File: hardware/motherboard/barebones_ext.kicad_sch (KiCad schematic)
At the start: 30 parts, among them J24 FH12-30S-0.5SH_55_, SW1 EC05E1220401, SW2 EC05E1220401, SW3 EC05E1220401, U36 STM32F411CEU6

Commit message: arranged the schematics in every sheet
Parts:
- removed R203: 100k, Resistor_SMD:R_0603_1608Metric, symbol Device:R
- removed R225: 1k, Resistor_SMD:R_0603_1608Metric, symbol Device:R
- removed R236: 10k, Resistor_SMD:R_0603_1608Metric, symbol Device:R
- removed S5: TL3342F160QG, barebones:SW_TL3342F160QG, symbol TL3342F160QG:TL3342F160QG
- added C419: 4.7uF, Capacitor_SMD:C_0603_1608Metric, symbol Device:C
- added C422, C424, C430, C434, C465, C467: 0.1uF, Capacitor_SMD:C_0603_1608Metric, symbol Device:C
- added C435, C466: 10uF, Capacitor_SMD:C_0603_1608Metric, symbol Device:C
- added C601, C602: 12pF, Capacitor_SMD:C_0201_0603Metric, symbol Device:C
- added R249, R250: 10k, Resistor_SMD:R_0603_1608Metric, symbol Device:R
- added SW4, SW6: SW_Push, symbol Switch:SW_Push
- added TP2: 3V3, TestPoint:TestPoint_Pad_D1.0mm, symbol Connector:TestPoint
- added TP3: BOOT0, TestPoint:TestPoint_Pad_D1.0mm, symbol Connector:TestPoint
- added TP4: NRST, TestPoint:TestPoint_Pad_D1.0mm, symbol Connector:TestPoint
- added TP7: SWDIO, TestPoint:TestPoint_Pad_D1.0mm, symbol Connector:TestPoint
- added TP8: SWCLK, TestPoint:TestPoint_Pad_D1.0mm, symbol Connector:TestPoint
- added Y8: C2E-25.000-10-1530-X-R, barebones:XTAL_C2E-25.000-10-1530-X-R, symbol C2E-25.000-10-1530-X-R:C2E-25.000-10-1530-X-R
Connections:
- net DC/SCL is gone; now on net SPI_SCK: U36.15 (PA5)
- net SDA is gone; now on net SPI_MOSI: U36.17 (PA7)
- net VDD is gone; now on net VCC_3V3_SYS: U36.24 (VDD), U36.36 (VDD), U36.48 (VDD)
- net BOOT0: now also R249.2, SW4.1, TP3.1
- net EN_BTN_0: now also U36.39 (PB3); no longer R233.1, R238.1, SW2.5, SW3.5
- net EN_CHAN_A_0: now also U36.19 (PB1)
- net EN_CHAN_A_1: now also U36.41 (PB5)
- net EN_CHAN_A_2: now also U36.45 (PB8)
- net EN_CHAN_B_0: now also U36.18 (PB0)
- net EN_CHAN_B_1: now also U36.40 (PB4)
- net EN_CHAN_B_2: now also U36.43 (PB7)
- net GND: now also C419.2, C422.2, C424.2, C430.2, C434.2, C435.2, C465.2, C466.2, C467.2, C601.1, C602.1, R249.1, R250.1, SW6.2, Y8.2 (GND), Y8.4 (GND)
- net LED_CS: now also U36.14 (PA4)
- net LED_DC: now also U36.13 (PA3)
- net LED_RES: now also U36.12 (PA2)
- net PRG_BTN_0: now also U36.21 (PB10)
- net PRG_BTN_1: now also U36.25 (PB12)
- net PRG_BTN_2: now also U36.26 (PB13)
- net VCC_3V3_SYS: now also U36.1 (VBAT), U36.9 (VREF+), C424.1, C430.1, C434.1, C435.1, C465.1, C466.1, C467.1, SW4.2, TP2.1
- net at U36.10 (PA0-WKUP): now also R250.2
- net at U36.22 (VCAP_1): now also C419.1
- net USB_VBUS: now reaches U36.30 (PA9)
- net USB_MACRO_DN: now reaches U36.32 (PA11)
- net USB_MACRO_DP: now reaches U36.33 (PA12)
- net SWDIO: now reaches U36.34 (PA13)
- net SWDIO: now also TP7.1
- net SWCLK: now reaches U36.37 (PA14)
- net SWCLK: now also TP8.1
- net EN_BTN_1: now reaches U36.42 (PB6)
- net EN_BTN_1: now also R233.1, SW2.5
- net EN_BTN_2: now reaches U36.46 (PB9)
- net EN_BTN_2: now also R238.1, SW3.5
- net XTALI: now reaches U36.5 (PH0-OSC_IN)
- net XTALI: now also C601.2, Y8.3
- net XTALO: now reaches U36.6 (PH1-OSC_OUT)
- net XTALO: now also C602.2, Y8.1
- net NRST: now reaches U36.7 (NRST)
- net NRST: now also C422.1, SW6.1, TP4.1
- no-connect marks 10 -> 20
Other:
- note added: "1.9" DISPLAY CONNECTOR"
- note added: "STM32F411 MCU"
- note added: "VDD CAPS"
- note added: "VREF+ CAPS"
- note removed: "POWER BUTTON"
- moved on the sheet: C409, C410, C416, C417, C421, J24, R137, R139, R142, R228, R229, R230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

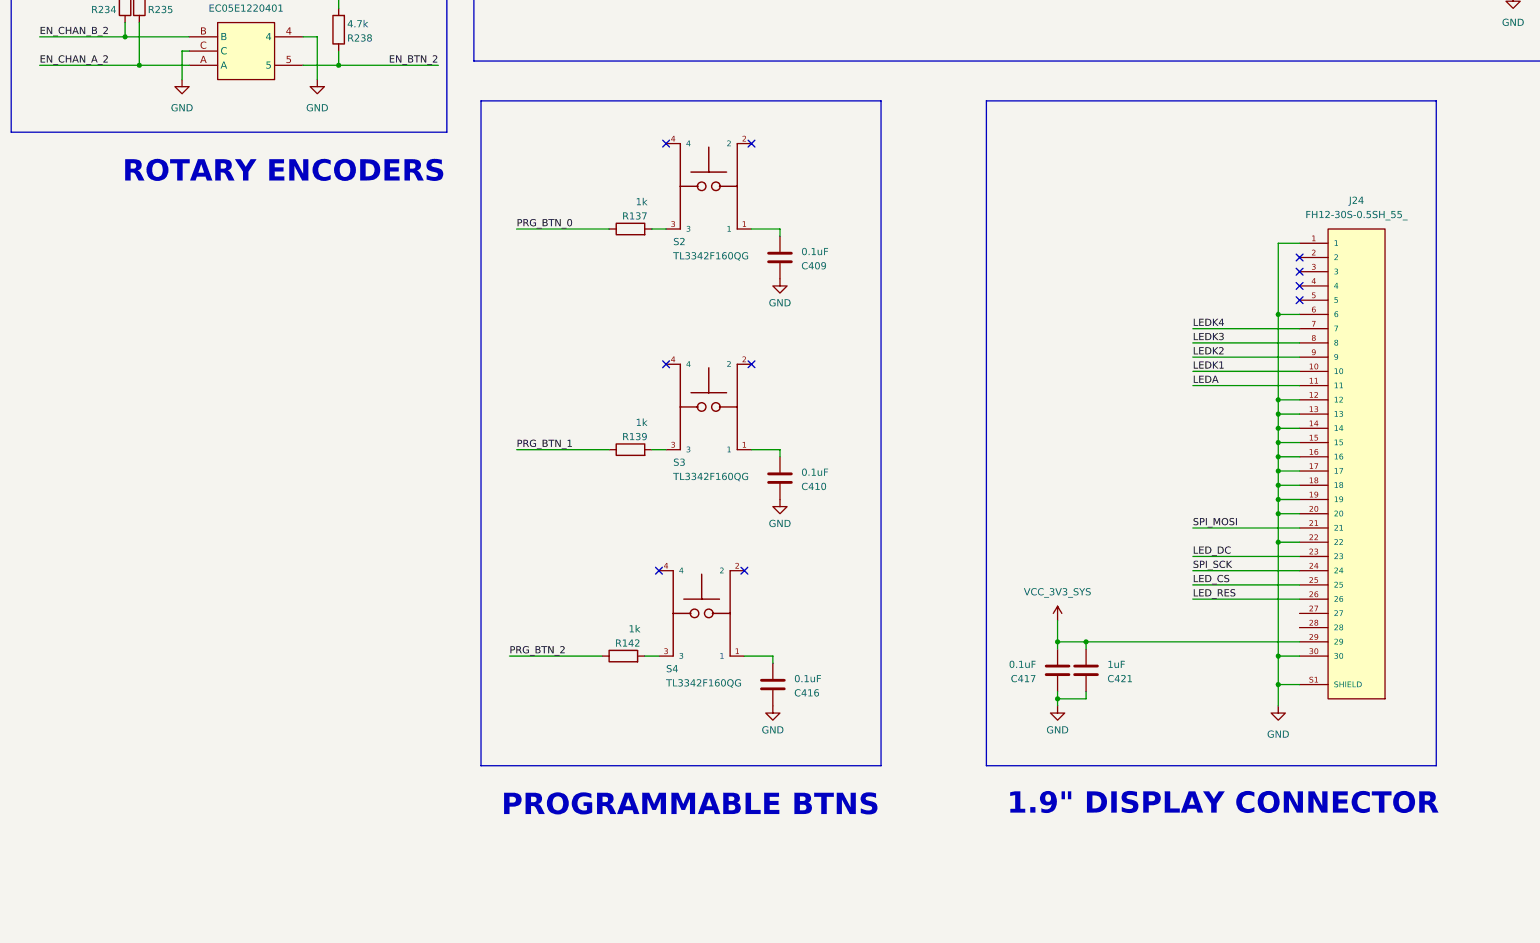
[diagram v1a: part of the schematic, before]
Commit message: removed unused components and connections
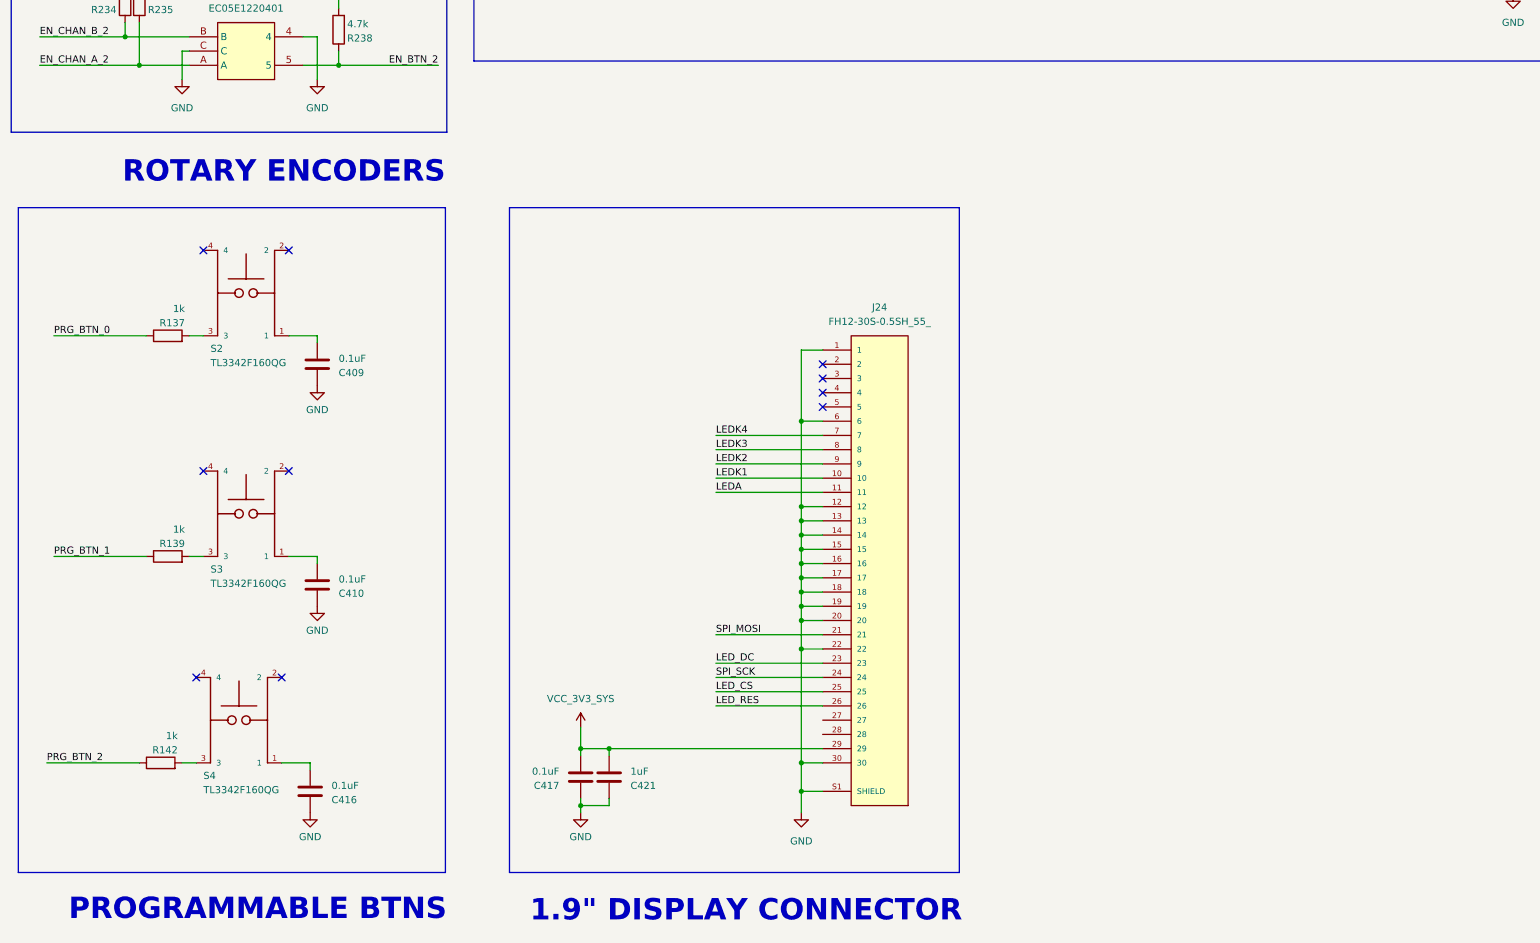
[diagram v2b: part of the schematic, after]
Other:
- moved on the sheet: C409, C410, C416, C417, C421, J24, R137, R139, R142, S2, S3, S4

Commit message: updated last changes
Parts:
- removed C417: 0.1uF, Capacitor_SMD:C_0603_1608Metric, symbol Device:C
- removed C421: 1uF, Capacitor_SMD:C_0603_1608Metric, symbol Device:C
- removed C601: 12pF, Capacitor_SMD:C_0201_0603Metric, symbol Device:C
- removed R228: 4.7k, Resistor_SMD:R_0402_1005Metric, symbol Device:R
- removed SW4, SW6: SW_Push, symbol Switch:SW_Push
- added C539: 0.1uF, Capacitor_SMD:C_0201_0603Metric, symbol Device:C
- added C546: 1uF, Capacitor_SMD:C_0201_0603Metric, symbol Device:C
- added C623: 12pF, Capacitor_SMD:C_0201_0603Metric, symbol Device:C
- added R236: 4.7k, Resistor_SMD:R_0201_0603Metric, symbol Device:R
- added S5, S6: TL3342F160QG, barebones:SW_TL3342F160QG, symbol TL3342F160QG:TL3342F160QG
- C409, C410, C416, C419, C422, C424, C430, C434, C465, C466, C467: footprint Capacitor_SMD:C_0603_1608Metric -> Capacitor_SMD:C_0201_0603Metric
- C435: value 10uF -> 0.1uF; footprint Capacitor_SMD:C_0603_1608Metric -> Capacitor_SMD:C_0201_0603Metric
- C602: KiLib_Generator (none) -> SMD_2terminal_chip_molded
- J24: footprint FH12-30S-0.5SH_55_:HIROSE_FH12-30S-0.5SH_55_ -> barebones:HIROSE_FH12-30S-0.5SH_55_
- R137, R139, R142, R237, R249, R250: footprint Resistor_SMD:R_0603_1608Metric -> Resistor_SMD:R_0201_0603Metric
- R229, R230, R231, R232, R233, R234, R235, R238: footprint Resistor_SMD:R_0402_1005Metric -> Resistor_SMD:R_0201_0603Metric
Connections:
- net LEDK2 is gone; now on net GND: J24.9
- net LEDK3 is gone; now on net SPI_DC: J24.8
- net USB_VBUS is gone; now on net EN_CHAN_A_0: U36.30 (PA9)
- net BOOT0: now also S6.3
- net EN_BTN_0: now also U36.31 (PA10); no longer U36.39 (PB3)
- net EN_BTN_1: now also U36.41 (PB5); no longer U36.42 (PB6)
- net EN_BTN_2: now also R234.1, U36.21 (PB10); no longer R238.1, U36.46 (PB9)
- net EN_CHAN_A_0: no longer U36.19 (PB1)
- net EN_CHAN_A_1: now also U36.40 (PB4); no longer U36.41 (PB5)
- net EN_CHAN_A_2: now also U36.46 (PB9); no longer U36.45 (PB8)
- net EN_CHAN_B_0: now also U36.29 (PA8), R236.1; no longer U36.18 (PB0)
- net EN_CHAN_B_1: now also U36.39 (PB3); no longer U36.40 (PB4)
- net EN_CHAN_B_2: now also R238.1, U36.45 (PB8); no longer R234.1, U36.43 (PB7)
- net GND: now also J24.11, J24.25, C539.2, C546.2, C623.1, S5.1; no longer J24.19, J24.20, J24.22, J24.6
- net LEDA: now also J24.20; no longer J24.11
- net NRST: now also S5.3
- net PRG_BTN_0: now also U36.25 (PB12); no longer U36.21 (PB10)
- net PRG_BTN_1: now also U36.26 (PB13); no longer U36.25 (PB12)
- net PRG_BTN_2: now also U36.27 (PB14); no longer U36.26 (PB13)
- net XTALI: now also C623.2
- net VCC_3V3_S3: now reaches J24.2
- net VCC_3V3_S3: now also C424.1, C430.1, C434.1, C435.1, C465.1, C466.1, C467.1, J24.3, J24.4, R229.2, R230.2, R231.2, R232.2, R233.2, R234.2, R235.2, R238.2, TP2.1, U36.1 (VBAT), U36.24 (VDD), U36.36 (VDD), U36.48 (VDD), U36.9 (VREF+), C539.1, C546.1, R236.2, S6.1
- net CTP_SCL: now reaches J24.27
- net CTP_SCL: now also U36.42 (PB6)
- net CTP_SDA: now reaches J24.28
- net CTP_SDA: now also U36.43 (PB7)
- net RESET: now reaches J24.5
- net RESET: now also U36.12 (PA2)
- net SPI_DC: now reaches U36.16 (PA6)
- net LEDK1 renamed MOSI
- net MOSI: now also U36.17 (PA7)
- net LEDK4 renamed SCLK
- net SCLK: now also U36.15 (PA5)
- net LED_CS renamed CS
- net CS: now also J24.6; no longer J24.25
- net LED_DC: no longer names the net of J24.23
- net LED_DC: no longer U36.13 (PA3)
- net LED_RES renamed CTP_RST
- net CTP_RST: now also U36.19 (PB1); no longer U36.12 (PA2)
- net SPI_MOSI: no longer names the net of J24.21
- net SPI_MOSI: no longer U36.17 (PA7)
- net SPI_SCK: no longer names the net of J24.24
- net SPI_SCK: no longer U36.15 (PA5)
- removed net VCC_3V3_SYS: C424.1, C430.1, C434.1, C435.1, C465.1, C466.1, C467.1, J24.29, R229.2, R230.2, R231.2, R232.2, R233.2, R234.2, R235.2, R238.2, TP2.1, U36.1 (VBAT), U36.24 (VDD), U36.36 (VDD), U36.48 (VDD), U36.9 (VREF+)
- new net CTP_INT: J24.29, U36.18 (PB0)
- new net LEDK: J24.22
- no-connect marks 20 -> 21
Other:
- note added: "ER-TFT019-1"
- moved on the sheet: C422, C602, J24, R249, Y8

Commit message: started routing on LPDDR4x RAM
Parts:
- removed R234, R235, R238: 4.7k, Resistor_SMD:R_0201_0603Metric, symbol Device:R
- removed SW3: EC05E1220401, barebones:SW-SMD_EC05E1220401, symbol EC05E1220401:EC05E1220401
- removed TP2: 3V3, TestPoint:TestPoint_Pad_D1.0mm, symbol Connector:TestPoint
- removed TP3: BOOT0, TestPoint:TestPoint_Pad_D1.0mm, symbol Connector:TestPoint
- removed TP4: NRST, TestPoint:TestPoint_Pad_D1.0mm, symbol Connector:TestPoint
- removed TP7: SWDIO, TestPoint:TestPoint_Pad_D1.0mm, symbol Connector:TestPoint
- removed TP8: SWCLK, TestPoint:TestPoint_Pad_D1.0mm, symbol Connector:TestPoint
- added J13: BM04B-SRSS-TB_LF__SN_, barebones:JST_BM04B-SRSS-TB_LF__SN_, symbol BM04B-SRSS-TB_LF__SN_:BM04B-SRSS-TB_LF__SN_
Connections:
- net GND: now also J13.4, J13.S1 (SHIELD), J13.S2 (SHIELD)
- net SWCLK: now also J13.3
- net SWDIO: now also J13.2
- net VCC_3V3_S3: now also J13.1
- net EN_BTN_2: no longer names the net of U36.21 (PB10)
- net EN_CHAN_A_2: no longer names the net of U36.46 (PB9)
- net EN_CHAN_B_2: no longer names the net of U36.45 (PB8)
- no-connect marks 21 -> 24
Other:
- moved on the sheet: C422, C602, C623, R249, S5, S6, Y8
